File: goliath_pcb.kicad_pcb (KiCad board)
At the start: 2 copper layers, 128.3 x 66 mm, 34 parts, among them IC1 MCT9001SD, IC2 MCT9001SD, IC3 MCT9001SD, IC4 MCT9001SD, IC5 MCT9001SD, IC6 LTC1298CS8-PBF, J1 RJ45_LED, J2 RJ45_LED, U1 Pico, U2 LM7805_TO220

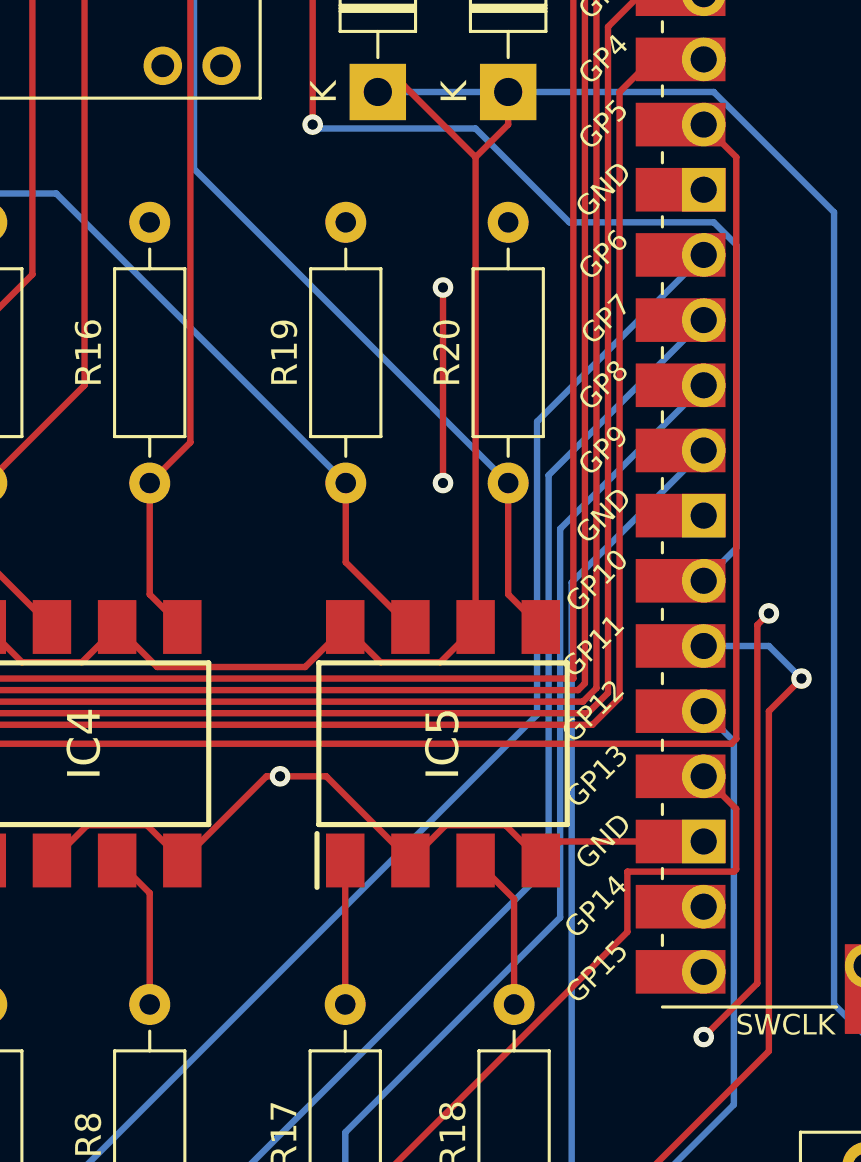
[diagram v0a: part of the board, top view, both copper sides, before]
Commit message: Move IC5 in line with other chips to avoid overlapping silkscreen
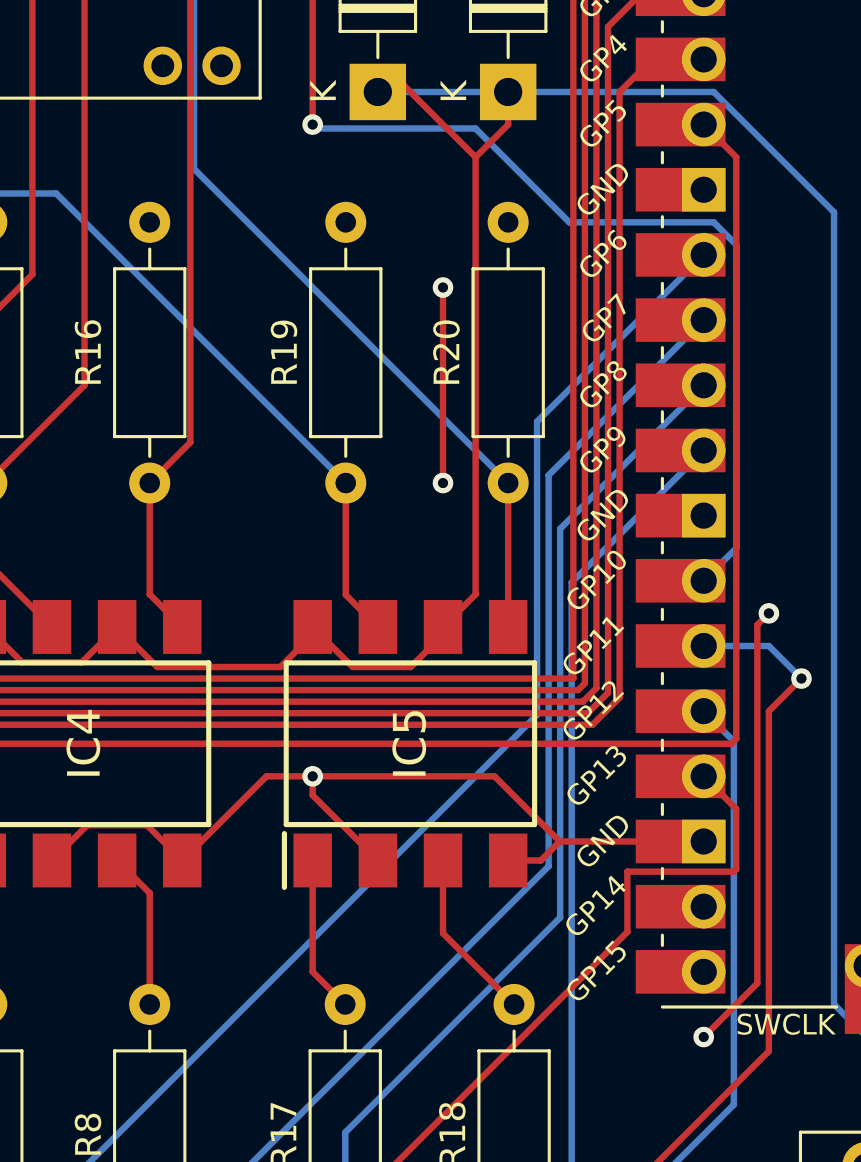
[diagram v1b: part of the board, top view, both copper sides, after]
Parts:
- moved IC5 1.27 mm to (162.6, 86.4)
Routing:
- net GND: track 81.9 -> 86.7 mm
- net Net-(IC5-Pad1): track 5.61 -> 6.14 mm
- net Net-(IC5-Pad7): track 50.6 -> 50.0 mm
- net Net-(IC5-Pad3): track 6.23 -> 6.76 mm
- net Net-(IC5-Pad5): track 41.4 -> 40.9 mm

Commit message: Remove extra text
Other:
- board text removed: "TODO: Encoder logic & connections"
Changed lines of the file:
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@@
   )
   (gr_rect (start 102.87 110.49) (end 231.14 44.45) (layer "Edge.Cuts") (width 0.1) (fill none))
-  (gr_text "TODO: Encoder logic & connections" (at 210.82 104.14) (layer "F.SilkS")
-    (effects (font (size 1 1) (thickness 0.15)))
-  )
   (segment (start 107.72 91.14) (end 107.95 90.91) (width 0.25) (layer "F.Cu") (net 1))
   (segment (start 107.72 96.52) (end 107.72 91.14) (width 0.25) (layer "F.Cu") (net 1))

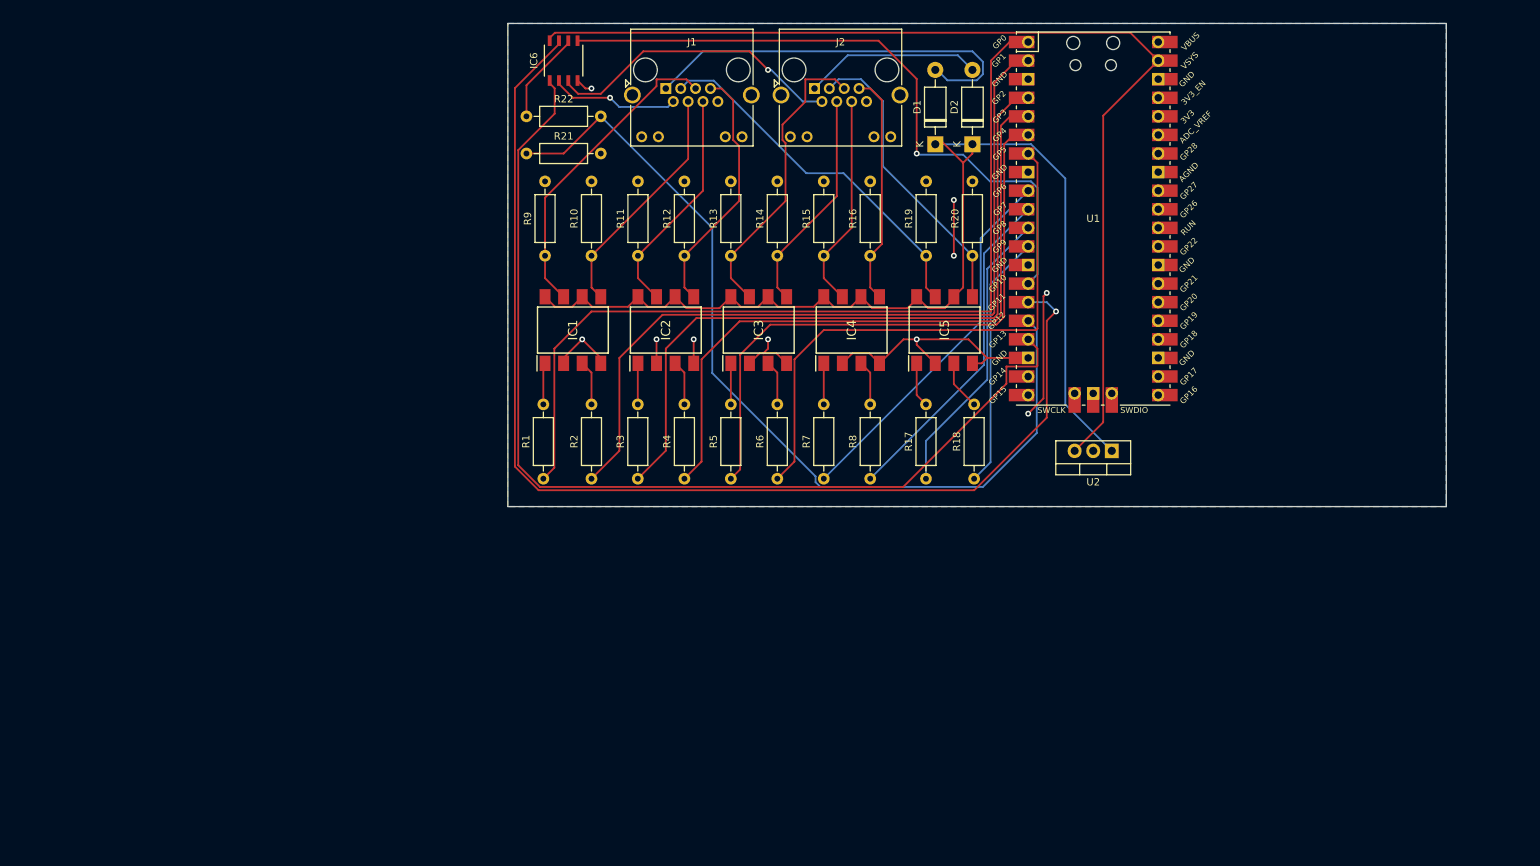
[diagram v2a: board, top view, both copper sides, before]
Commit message: Add buffers, restart PCB layout, start encoder stuff
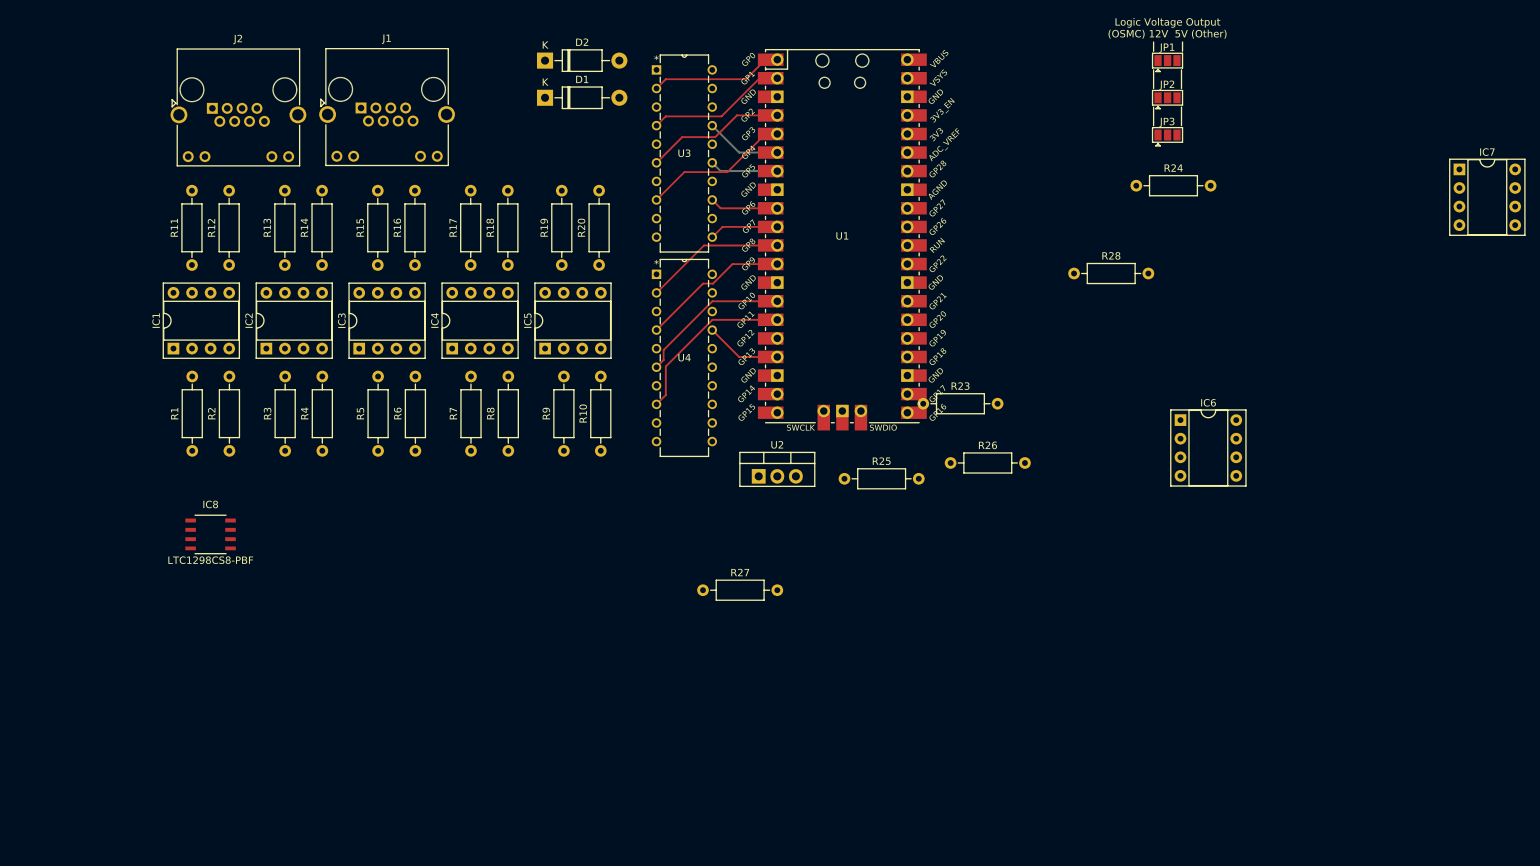
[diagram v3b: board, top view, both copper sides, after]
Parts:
- removed R21: 3.3k, Resistor_THT:R_Axial_DIN0207_L6.3mm_D2.5mm_P10.16mm_Horizontal
- removed R22: 1.7k, Resistor_THT:R_Axial_DIN0207_L6.3mm_D2.5mm_P10.16mm_Horizontal
- added IC7: MCT9001SD, Package_DIP:DIP-8_W7.62mm_Socket, F.Cu at (232.9, 64.4)
- added IC8: LTC1298CS8-PBF, LTC1298:LTC1298CS8-PBF, F.Cu at (62.2, 114.3)
- added JP1: SolderJumper_3_Bridged12, Jumper:SolderJumper-3_P1.3mm_Open_Pad1.0x1.5mm, F.Cu at (193.0, 49.5)
- added JP2: SolderJumper_3_Bridged12, Jumper:SolderJumper-3_P1.3mm_Open_Pad1.0x1.5mm, F.Cu at (193.0, 54.6)
- added JP3: SolderJumper_3_Bridged12, Jumper:SolderJumper-3_P1.3mm_Open_Pad1.0x1.5mm, F.Cu at (193.0, 59.7)
- added R23: 470, Resistor_THT:R_Axial_DIN0207_L6.3mm_D2.5mm_P10.16mm_Horizontal, F.Cu at (159.7, 96.4)
- added R24: 470, Resistor_THT:R_Axial_DIN0207_L6.3mm_D2.5mm_P10.16mm_Horizontal, F.Cu at (188.8, 66.6)
- added R25: 2k, Resistor_THT:R_Axial_DIN0207_L6.3mm_D2.5mm_P10.16mm_Horizontal, F.Cu at (148.9, 106.7)
- added R26: 2k, Resistor_THT:R_Axial_DIN0207_L6.3mm_D2.5mm_P10.16mm_Horizontal, F.Cu at (163.4, 104.5)
- added R27: 2k, Resistor_THT:R_Axial_DIN0207_L6.3mm_D2.5mm_P10.16mm_Horizontal, F.Cu at (129.5, 121.9)
- added R28: 2k, Resistor_THT:R_Axial_DIN0207_L6.3mm_D2.5mm_P10.16mm_Horizontal, F.Cu at (180.3, 78.6)
- added U3: 74HCT244, 74HCT241:CD74HCT241E, F.Cu at (130.8, 73.7)
- added U4: 74HCT244, 74HCT241:CD74HCT241E, F.Cu at (130.8, 101.6)
- IC1, IC2, IC3, IC4, IC5: footprint MCT9001:SOP254P1016X385-8N -> Package_DIP:DIP-8_W7.62mm_Socket
- IC6: value LTC1298CS8-PBF -> MCT9001SD; footprint footprints:LTC1298CS8-PBF -> Package_DIP:DIP-8_W7.62mm_Socket
- R10, R9: value 2k -> 470
- R17, R18: value 470 -> 2k
- moved IC6 97.6 mm to (194.8, 98.7), turned to 0 degrees
- moved J2 82.3 mm to (62.5, 56.1)
- moved R18 70.1 mm to (102.9, 77.5)
- moved R17 68.7 mm to (97.8, 77.5)
- moved R12 62.2 mm to (64.8, 77.5)
- moved R16 62.2 mm to (90.2, 77.5)
- moved R14 62.2 mm to (77.5, 77.5)
- moved R11 61.0 mm to (59.7, 77.5)
- moved R15 61.0 mm to (85.1, 77.5)
- moved R13 61.0 mm to (72.4, 77.5)
- moved D2 59.5 mm to (108.0, 49.5), turned to 0 degrees
- moved IC3 54.7 mm to (82.5, 88.9)
- moved IC1 54.7 mm to (57.2, 88.9)
- moved IC4 54.7 mm to (95.3, 88.9)
- moved IC5 54.7 mm to (108.0, 88.9)
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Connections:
- IC1 pad 6: 12V -> LGV
- IC1 pad 8: 12V -> LGV
- IC2 pad 6: 12V -> LGV
- IC2 pad 8: 12V -> LGV
- IC3 pad 6: 12V -> LGV
- IC3 pad 8: 12V -> LGV
- IC4 pad 6: 12V -> LGV
- IC4 pad 8: 12V -> LGV
- IC5 pad 6: 12V -> LGV
- IC5 pad 8: 12V -> LGV
- IC6 pad 2: Net-(IC6-Pad2) -> GND
- IC6 pad 5: Net-(IC6-Pad5) -> Net-(IC8-Pad7)
- IC6 pad 6: Net-(IC6-Pad6) -> unconnected-(IC6-Pad6)
- IC6 pad 7: Net-(IC6-Pad7) -> Net-(IC8-Pad5)
- J1 pad 1: Net-(D1-Pad2) -> Net-(J1-Pad1)
- J1 pad 2: Net-(IC6-Pad2) -> Net-(IC8-Pad2)
- J2 pad 1: Net-(D2-Pad2) -> Net-(J2-Pad1)
- J2 pad 2: Net-(IC6-Pad3) -> Net-(J2-Pad2)
- R10 pad 1: Net-(IC1-Pad5) -> Net-(R10-Pad1)
- R10 pad 2: GND -> Net-(IC5-Pad3)
- R11 pad 1: Net-(IC2-Pad7) -> Net-(IC1-Pad7)
- R12 pad 1: Net-(IC2-Pad5) -> Net-(IC1-Pad5)
- R13 pad 1: Net-(IC3-Pad7) -> Net-(IC2-Pad7)
- R14 pad 1: Net-(IC3-Pad5) -> Net-(IC2-Pad5)
- R15 pad 1: Net-(IC4-Pad7) -> Net-(IC3-Pad7)
- R16 pad 1: Net-(IC4-Pad5) -> Net-(IC3-Pad5)
- R17 pad 1: Net-(R17-Pad1) -> Net-(IC4-Pad7)
- R17 pad 2: Net-(IC5-Pad1) -> GND
- R18 pad 1: Net-(R18-Pad1) -> Net-(IC4-Pad5)
- R18 pad 2: Net-(IC5-Pad3) -> GND
- R9 pad 1: Net-(IC1-Pad7) -> Net-(R9-Pad1)
- R9 pad 2: GND -> Net-(IC5-Pad1)
- U1 pad 1: Net-(R1-Pad1) -> Net-(U1-Pad1)
- U1 pad 10: Net-(R8-Pad1) -> Net-(U1-Pad10)
- U1 pad 11: Net-(R17-Pad1) -> Net-(U1-Pad11)
- U1 pad 12: Net-(R18-Pad1) -> Net-(U1-Pad12)
- U1 pad 14: Net-(IC6-Pad5) -> Net-(U1-Pad14)
- U1 pad 15: Net-(IC6-Pad7) -> Net-(U1-Pad15)
- U1 pad 17: Net-(IC6-Pad1) -> Net-(U1-Pad17)
- U1 pad 2: Net-(R2-Pad1) -> Net-(U1-Pad2)
- U1 pad 4: Net-(R3-Pad1) -> Net-(U1-Pad4)
- U1 pad 5: Net-(R4-Pad1) -> Net-(U1-Pad5)
- U1 pad 6: Net-(R5-Pad1) -> Net-(U1-Pad6)
- U1 pad 7: Net-(R6-Pad1) -> Net-(U1-Pad7)
- U1 pad 9: Net-(R7-Pad1) -> Net-(U1-Pad9)
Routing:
- net Net-(IC6-Pad7): track 158.2 -> 0.00 mm, vias 1 -> 0
- net 12V: track 153.4 -> 0.00 mm
- net 5V: track 143.5 -> 0.00 mm
- net Net-(IC6-Pad1): track 139.5 -> 0.00 mm
- net Net-(U1-Pad16): track 123.8 -> 0.00 mm
- net Net-(R1-Pad1): track 120.6 -> 0.00 mm
- net Net-(R2-Pad1): track 109.2 -> 0.00 mm
- net Net-(R3-Pad1): track 98.9 -> 0.00 mm
- net Net-(R4-Pad1): track 90.9 -> 0.00 mm
- net Net-(IC6-Pad5): track 90.8 -> 0.00 mm, vias 1 -> 0
- net GND: track 86.7 -> 0.00 mm, vias 10 -> 0
- net Net-(R5-Pad1): track 83.1 -> 0.00 mm
- net Net-(R6-Pad1): track 76.7 -> 0.00 mm
- net Net-(D1-Pad2): track 55.3 -> 0.00 mm
- net Net-(R7-Pad1): track 50.9 -> 0.00 mm
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- removed copper zone on B.Cu, net GND
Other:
- board outline removed
- board text added: "Logic Voltage Output (OSMC) 12V 5V (Other)"

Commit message: Layout PCB
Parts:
- removed IC8: LTC1298CS8-PBF, LTC1298:LTC1298CS8-PBF
- added J3: RJ45_LED, Connector_RJ:RJ45_Amphenol_RJHSE538X, F.Cu at (44.5, 80.1)
- added J4: RJ45_LED, Connector_RJ:RJ45_Amphenol_RJHSE538X, F.Cu at (44.5, 100.7)
- added JP4: SolderJumper_3_Bridged12, Jumper:SolderJumper-3_P1.3mm_Open_Pad1.0x1.5mm, B.Cu at (63.5, 113.1)
- added R21: 470, Resistor_THT:R_Axial_DIN0207_L6.3mm_D2.5mm_P10.16mm_Horizontal, F.Cu at (94.0, 109.2)
- added R22: 470, Resistor_THT:R_Axial_DIN0207_L6.3mm_D2.5mm_P10.16mm_Horizontal, F.Cu at (94.0, 114.3)
- added R29: 10k, Resistor_THT:R_Axial_DIN0207_L6.3mm_D2.5mm_P10.16mm_Horizontal, F.Cu at (50.8, 118.1)
- added R30: 10k, Resistor_THT:R_Axial_DIN0207_L6.3mm_D2.5mm_P10.16mm_Horizontal, F.Cu at (55.9, 118.1)
- added R31: 10k, Resistor_THT:R_Axial_DIN0207_L6.3mm_D2.5mm_P10.16mm_Horizontal, F.Cu at (61.0, 118.1)
- added R32: 10k, Resistor_THT:R_Axial_DIN0207_L6.3mm_D2.5mm_P10.16mm_Horizontal, F.Cu at (66.0, 118.1)
- added R33: 10k, Resistor_THT:R_Axial_DIN0207_L6.3mm_D2.5mm_P10.16mm_Horizontal, F.Cu at (76.2, 118.1)
- added R34: 10k, Resistor_THT:R_Axial_DIN0207_L6.3mm_D2.5mm_P10.16mm_Horizontal, F.Cu at (71.1, 118.1)
- added U5: LTC1298CS8-PBF, Package_DIP:DIP-8_W7.62mm_Socket, F.Cu at (81.3, 108.0)
- JP1, JP2, JP3: moved to B.Cu
- R23, R24: value 470 -> 2k
- R25, R26: value 2k -> 470
- U3, U4: footprint 74HCT241:CD74HCT241E -> Package_DIP:DIP-20_W7.62mm_Socket
- moved JP1 162.8 mm to (43.2, 113.0), turned to -90 degrees
- moved JP2 156.1 mm to (48.3, 113.0), turned to -90 degrees
- moved JP3 149.5 mm to (53.3, 113.0), turned to -90 degrees
- moved IC7 96.1 mm to (147.3, 108.0)
- moved IC6 87.3 mm to (108.0, 108.0)
- moved R24 84.2 mm to (119.4, 114.3)
- moved R23 42.3 mm to (119.4, 109.3)
- moved R28 41.7 mm to (158.8, 114.3)
- moved R27 31.9 mm to (158.8, 109.2)
- moved R26 31.6 mm to (133.3, 114.3)
- moved U3 24.1 mm to (123.2, 50.8)
- moved U4 24.1 mm to (123.2, 78.7)
- moved D2 16.3 mm to (118.1, 62.2), turned to 90 degrees
- moved U2 15.2 mm to (138.9, 121.4), turned to 180 degrees
- moved D1 8.52 mm to (111.8, 62.2), turned to 180 degrees
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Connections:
- IC6 pad 5: Net-(IC8-Pad7) -> Net-(IC6-Pad5)
- IC6 pad 6: unconnected-(IC6-Pad6) -> 5V
- IC6 pad 7: Net-(IC8-Pad5) -> Net-(IC6-Pad7)
- IC7 pad 1: Net-(U4-Pad3) -> Net-(IC7-Pad1)
- IC7 pad 3: Net-(U4-Pad5) -> Net-(IC7-Pad3)
- JP1 pad 3: 5V -> Net-(JP1-Pad3)
- R23 pad 1: Net-(U4-Pad14) -> Net-(IC6-Pad7)
- R23 pad 2: Net-(IC6-Pad1) -> GND
- R24 pad 1: Net-(U4-Pad12) -> Net-(IC6-Pad5)
- R24 pad 2: Net-(IC6-Pad3) -> GND
- R25 pad 1: Net-(IC8-Pad5) -> Net-(IC7-Pad1)
- R25 pad 2: GND -> Net-(U4-Pad3)
- R26 pad 1: Net-(IC8-Pad7) -> Net-(U4-Pad5)
- R26 pad 2: GND -> Net-(IC7-Pad3)
- U1 pad 19: unconnected-(U1-Pad19) -> Net-(J3-Pad3)
- U1 pad 20: unconnected-(U1-Pad20) -> Net-(J3-Pad4)
- U1 pad 21: unconnected-(U1-Pad21) -> Net-(J4-Pad3)
- U1 pad 22: unconnected-(U1-Pad22) -> Net-(J4-Pad4)
- U4 pad 12: Net-(U4-Pad12) -> Net-(R22-Pad1)
- U4 pad 14: Net-(U4-Pad14) -> Net-(R21-Pad1)
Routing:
- net Net-(IC4-Pad3): track 0.00 -> 4.89 mm
- net Net-(IC3-Pad3): track 0.00 -> 4.89 mm
- net Net-(IC5-Pad1): track 0.00 -> 4.88 mm
- net Net-(IC2-Pad3): track 0.00 -> 4.88 mm
- net Net-(IC2-Pad1): track 0.00 -> 4.88 mm
- net Net-(IC1-Pad3): track 0.00 -> 4.88 mm
- net Net-(IC1-Pad1): track 0.00 -> 4.88 mm
- net Net-(IC4-Pad1): track 0.00 -> 4.88 mm
- net Net-(IC3-Pad1): track 0.00 -> 4.88 mm
- net Net-(IC5-Pad3): track 0.00 -> 4.87 mm
- net Net-(IC7-Pad1): track 0.00 -> 4.36 mm
- net Net-(IC7-Pad3): track 0.00 -> 4.34 mm
- net Net-(IC6-Pad1): track 0.00 -> 4.34 mm
- net Net-(IC6-Pad3): track 0.00 -> 4.34 mm
- net Net-(IC6-Pad7): track 0.00 -> 4.31 mm
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- added copper zone on B.Cu, net GND
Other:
- board outline added: 138.4 x 81.9 mm
- board text added: "5V 3v3"
- board text added: "Logic Voltage Output 12V 5/3v3"
- board text removed: "Logic Voltage Output (OSMC) 12V 5V (Other)"
